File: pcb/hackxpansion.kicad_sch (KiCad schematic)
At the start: 0 parts

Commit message: added mcu and adc
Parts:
- added R1, R2: 27, symbol Device:R
- added R4: 1k, Resistor_SMD:R_0402_1005Metric, symbol Device:R
- added SW1: SW_Push, symbol Switch:SW_Push
- added U1: ADS131M08xPBS, Package_QFP:TQFP-32_5x5mm_P0.5mm, symbol Analog_ADC:ADS131M08xPBS
- added U2: RP2354B, Package_DFN_QFN:QFN-80-1EP_10x10mm_P0.4mm_EP3.4x3.4mm, symbol MCU_RaspberryPi:RP2354B
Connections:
- new net: R1.1, U2.66 (USB_DM)
- new net: U1.13 (AGND), U1.27 (AGND), U1.28 (AGND)
- new net: R4.1, SW1.1
- new net: SW1.2, U2.35 (RUN)
- new net: R2.1, U2.67 (USB_DP)
- new net: U2.10 (DVDD), U2.32 (DVDD), U2.51 (DVDD)
- new net: U2.15 (IOVDD), U2.24 (IOVDD), U2.29 (IOVDD), U2.41 (IOVDD), U2.5 (IOVDD), U2.50 (IOVDD), U2.60 (IOVDD), U2.76 (IOVDD)
- new net USB_D+: R2.2
- new net USB_D-: R1.2

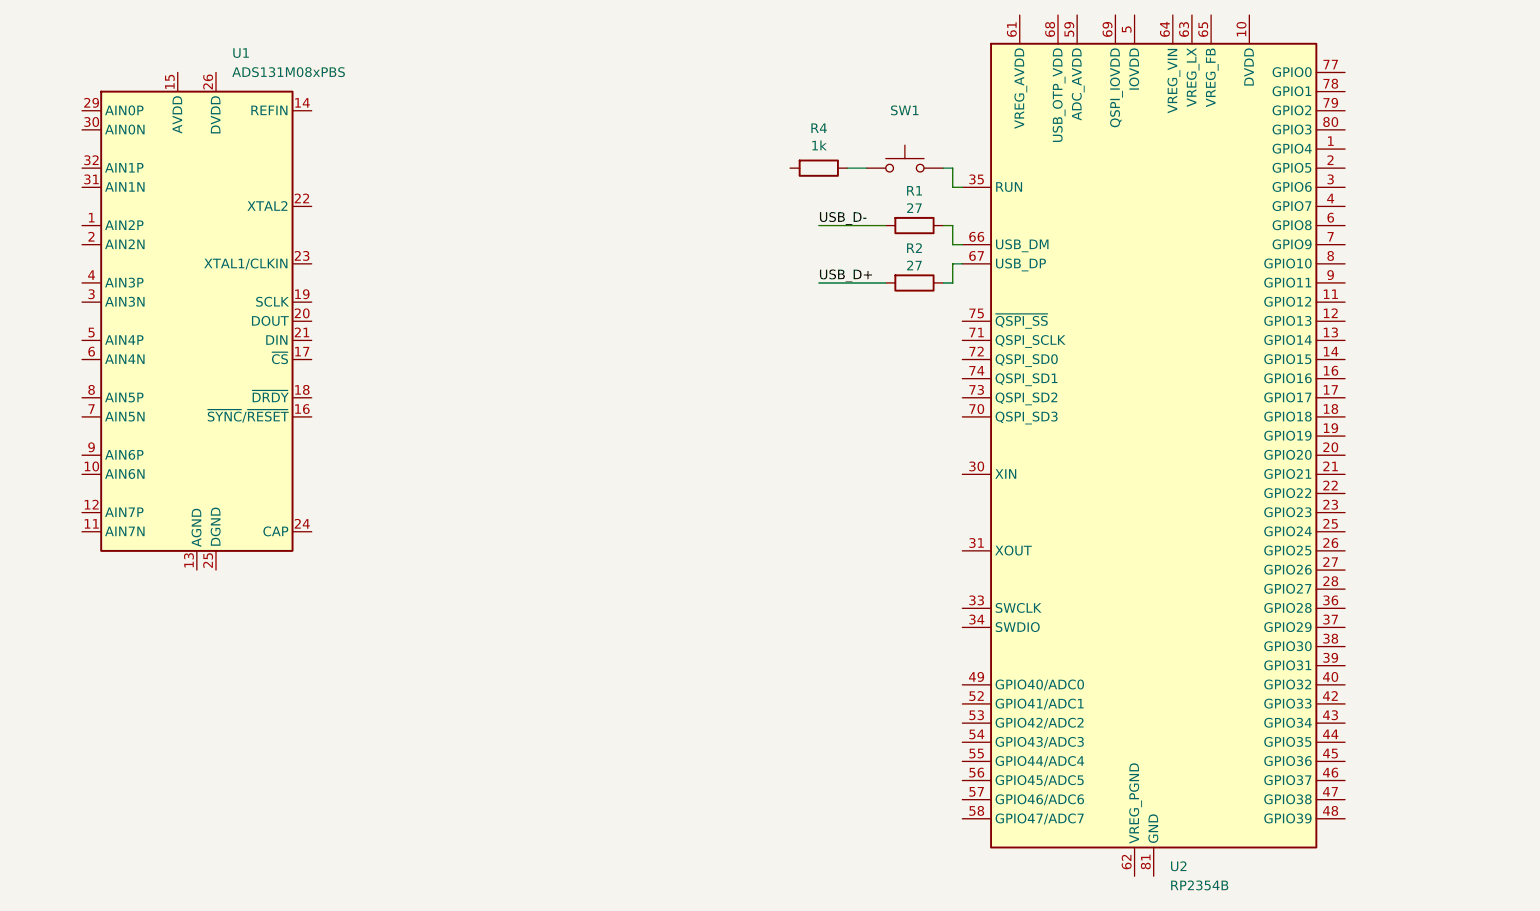
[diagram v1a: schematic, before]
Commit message: Added RP2354B and made basic fanout
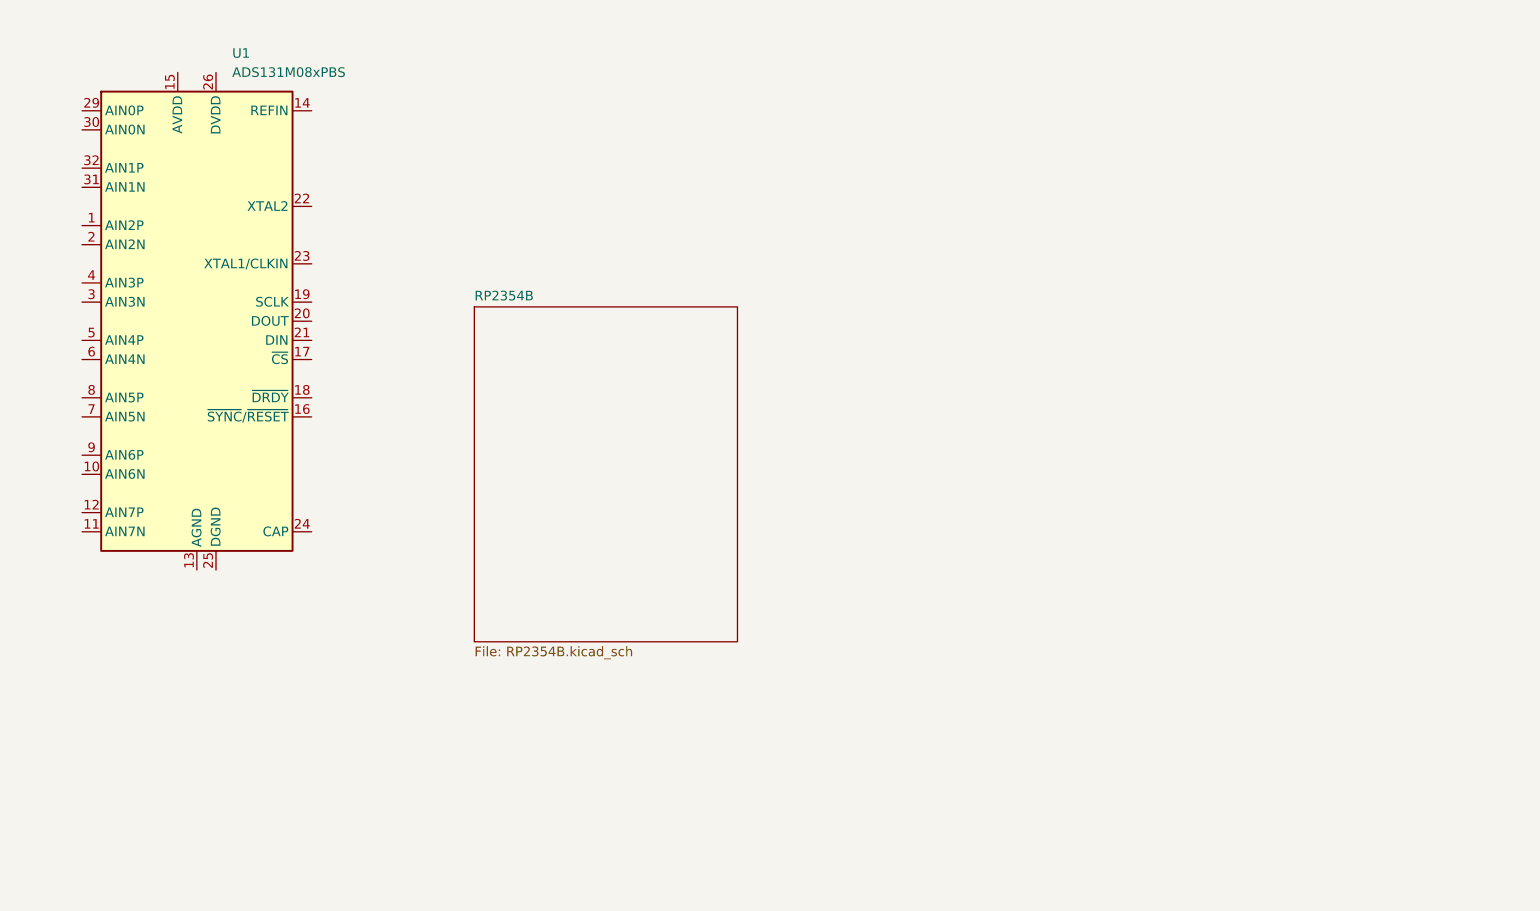
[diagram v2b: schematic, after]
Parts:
- removed R1, R2: 27, symbol Device:R
- removed R4: 1k, Resistor_SMD:R_0402_1005Metric, symbol Device:R
- removed SW1: SW_Push, symbol Switch:SW_Push
- removed U2: RP2354B, Package_DFN_QFN:QFN-80-1EP_10x10mm_P0.4mm_EP3.4x3.4mm, symbol MCU_RaspberryPi:RP2354B
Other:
- added sheet RP2354B (RP2354B.kicad_sch)

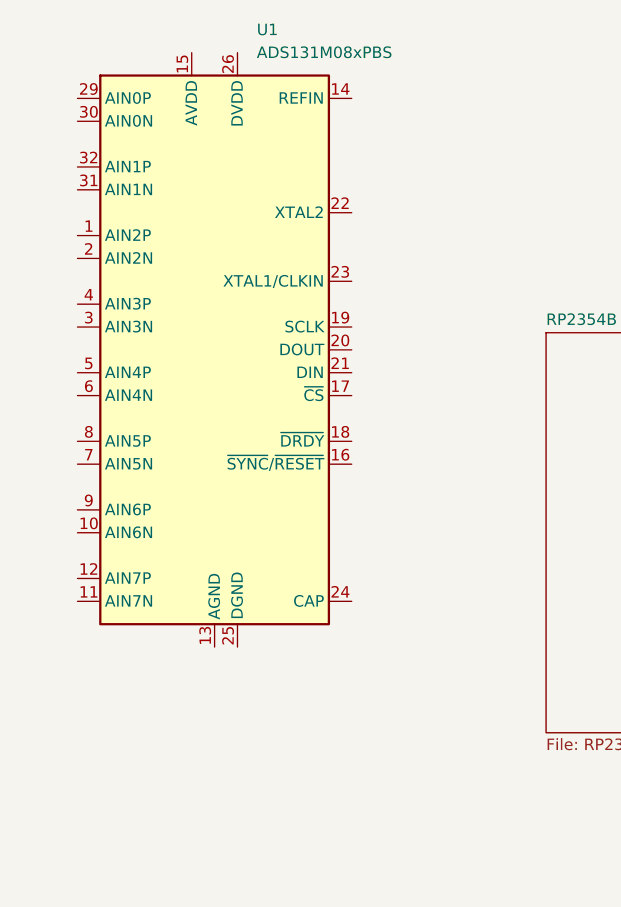
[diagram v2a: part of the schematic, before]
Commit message: Completed fanout
Completed the fanout for the rp2354B also placed the silkscreen labels in places where you can read them.
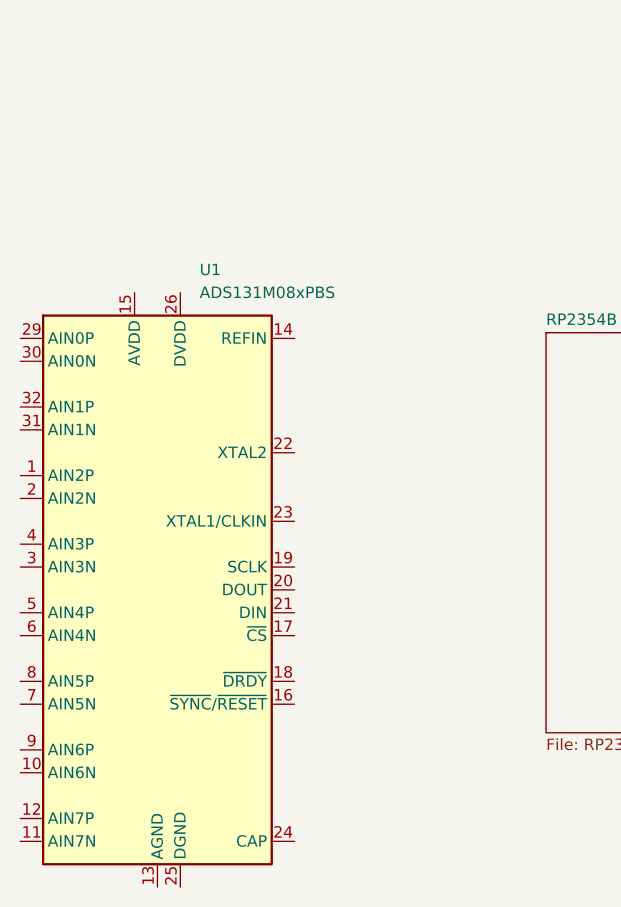
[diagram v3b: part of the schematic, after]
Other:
- moved on the sheet: U1
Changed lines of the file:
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@@
 	(symbol
 		(lib_id "Analog_ADC:ADS131M08xPBS")
-		(at 85.09 76.2 0)
+		(at 78.74 102.87 0)
 		(unit 1)
 		(exclude_from_sim no)
@@
 		(fields_autoplaced yes)
 		(property "Reference" "U1"
-			(at 89.7733 40.64 0)
+			(at 83.4233 67.31 0)
 			(effects
 				(font
@@
 		)
 		(property "Value" "ADS131M08xPBS"
-			(at 89.7733 43.18 0)
+			(at 83.4233 69.85 0)
 			(effects
 				(font
@@
 		)
 		(property "Footprint" "Package_QFP:TQFP-32_5x5mm_P0.5mm"
-			(at 135.89 132.08 0)
+			(at 129.54 158.75 0)
 			(effects
 				(font
@@
 		)
 		(property "Datasheet" "https://www.ti.com/lit/ds/symlink/ads131m08.pdf"
-			(at 135.89 134.62 0)
+			(at 129.54 161.29 0)
 			(effects
 				(font
@@
 		)
 		(property "Description" "8-channel, 24-bit, simultaneous sampling Delta-Sigma ADC, 32kSPS, G=1..128 PGA, SPI interface, integrated 1.2V reference, TQFP-32 (Texas PBS / S-PQFP-G32)"
-			(at 146.05 137.16 0)
+			(at 139.7 163.83 0)
 			(effects
 				(font

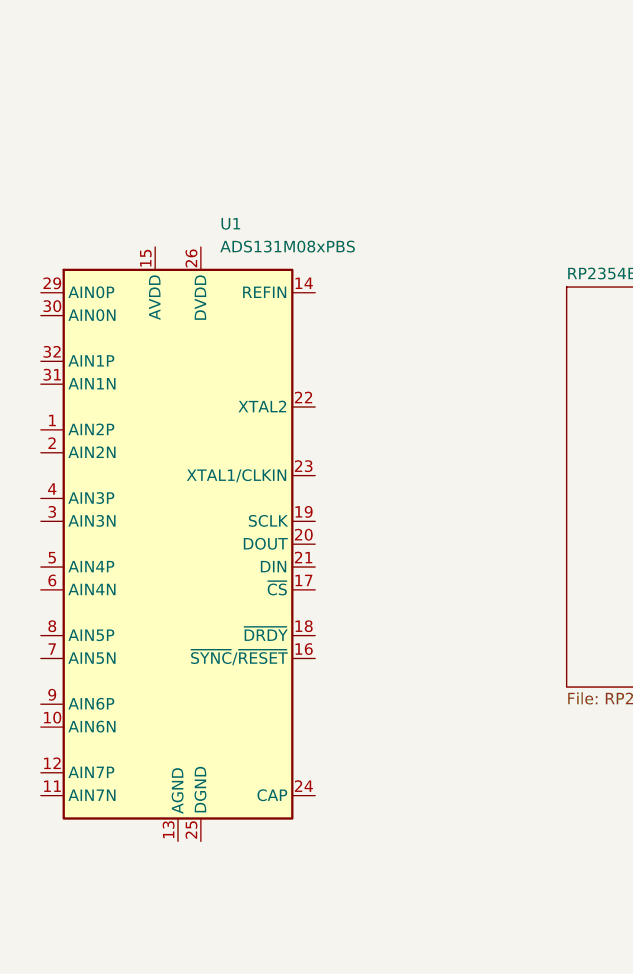
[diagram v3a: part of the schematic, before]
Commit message: ADC Power and input
Started with the power input and communication for the ADC
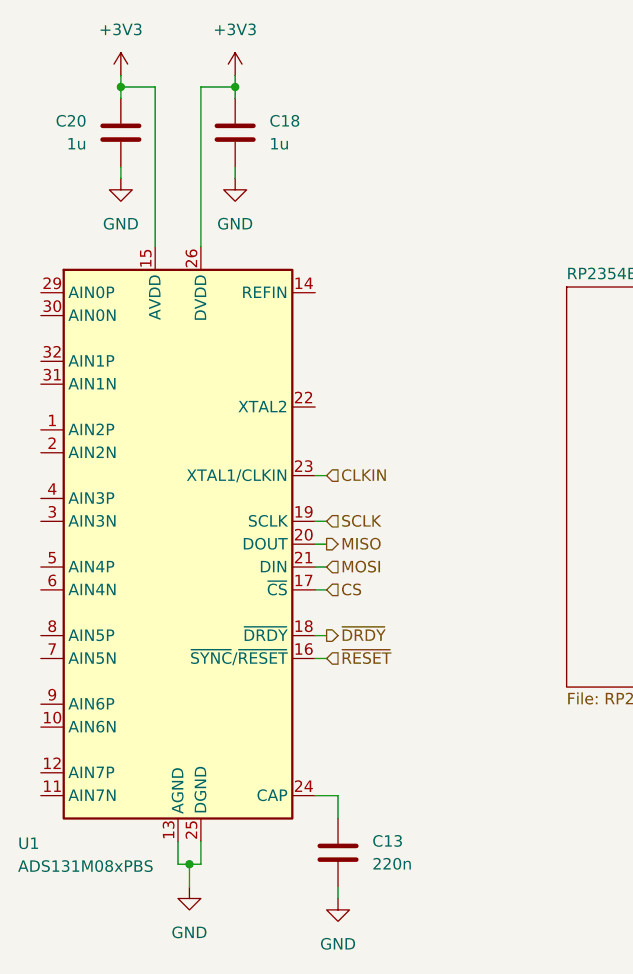
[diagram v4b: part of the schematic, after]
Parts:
- added C13: 220n, symbol Device:C
- added C18, C20: 1u, symbol Device:C
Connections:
- net GND: now reaches U1.13 (AGND), U1.27 (AGND), U1.28 (AGND)
- net GND: now also U1.25 (DGND), C13.2, C18.2, C20.2
- net +3V3: now reaches U1.15 (AVDD)
- net +3V3: now also U1.26 (DVDD), C18.1, C20.1
- net ~{RESET}: now reaches U1.16 (~{SYNC}/~{RESET})
- net CS: now reaches U1.17 (~{CS})
- net ~{DRDY}: now reaches U1.18 (~{DRDY})
- net SCLK: now reaches U1.19 (SCLK)
- net MISO: now reaches U1.20 (DOUT)
- net MOSI: now reaches U1.21 (DIN)
- net CLKIN: now reaches U1.23 (XTAL1/CLKIN)
- net at U1.24 (CAP): now also C13.1

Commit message: Fixed missing stuff and now finally separate sheet for the ADC
Auto stash before merge of "main" and "origin/main"
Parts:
- removed C13: 220n, symbol Device:C
- removed C18, C20: 1u, symbol Device:C
- removed U1: ADS131M08xPBS, Package_QFP:TQFP-32_5x5mm_P0.5mm, symbol Analog_ADC:ADS131M08xPBS
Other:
- added sheet ADC (ADC.kicad_sch)

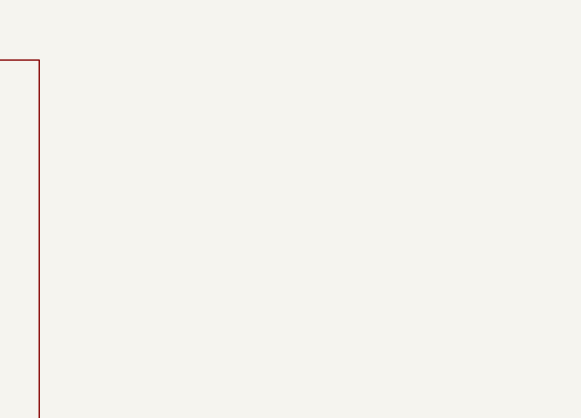
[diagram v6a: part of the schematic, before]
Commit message: added new adc symbol
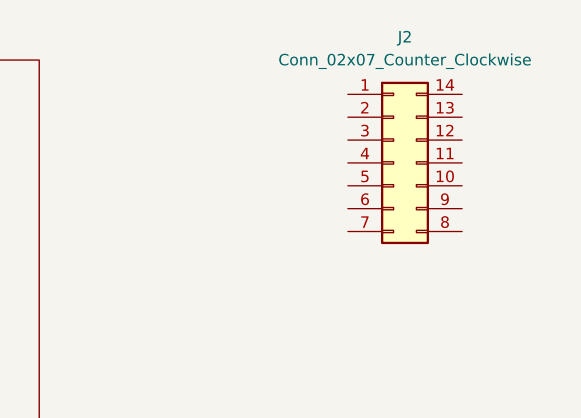
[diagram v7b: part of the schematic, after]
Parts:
- added J2: Conn_02x07_Counter_Clockwise, Connector_PinSocket_2.54mm:PinSocket_2x07_P2.54mm_Horizontal, symbol Connector_Generic:Conn_02x07_Counter_Clockwise
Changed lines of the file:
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@@
 	(generator_version "10.0")
 	(paper "A4")
+	(symbol
+		(lib_id "Connector_Generic:Conn_02x07_Counter_Clockwise")
+		(at 242.57 87.63 0)
+		(unit 1)
+		(body_style 1)
+		(exclude_from_sim no)
+		(in_bom yes)
+		(on_board yes)
+		(in_pos_files yes)
+		(dnp no)
+		(fields_autoplaced yes)
+		(property "Reference" "J2"
+			(at 243.84 73.66 0)
+			(show_name no)
+			(do_not_autoplace no)
+			(effects
+				(font
+					(size 1.27 1.27)
+				)
+			)
+		)
+		(property "Value" "Conn_02x07_Counter_Clockwise"
+			(at 243.84 76.2 0)
+			(show_name no)
+			(do_not_autoplace no)
+			(effects
+				(font
+					(size 1.27 1.27)
+				)
+			)
+		)
+		(property "Footprint" "Connector_PinSocket_2.54mm:PinSocket_2x07_P2.54mm_Horizontal"
+			(at 242.57 87.63 0)
+			(hide yes)
+			(show_name no)
+			(do_not_autoplace no)
+			(effects
+				(font
+					(size 1.27 1.27)
+				)
+			)
+		)
+		(property "Datasheet" ""
+			(at 242.57 87.63 0)
+			(hide yes)
+			(show_name no)
+			(do_not_autoplace no)
+			(effects
+				(font
+					(size 1.27 1.27)
+				)
+			)
+		)
+		(property "Description" "Generic connector, double row, 02x07, counter clockwise pin numbering scheme (similar to DIP package numbering), script generated (kicad-library-utils/schlib/autogen/connector/)"
+			(at 242.57 87.63 0)
+			(hide yes)
+			(show_name no)
+			(do_not_autoplace no)
+			(effects
+				(font
+					(size 1.27 1.27)
+				)
+			)
+		)
+		(pin "4"
+		)
+		(pin "10"
+		)
+		(pin "1"
+		)
+		(pin "11"
+		)
+		(pin "3"
+		)
+		(pin "2"
+		)
+		(pin "7"
+		)
+		(pin "9"
+		)
+		(pin "12"
+		)
+		(pin "14"
+		)
+		(pin "5"
+		)
+		(pin "13"
+		)
+		(pin "8"
+		)
+		(pin "6"
+		)
+		(instances
+			(project "hackxpansion"
+				(path "/aaf5804d-3f78-442b-969e-39faa388db94"
+					(reference "J2")
+					(unit 1)
+				)
+			)
+		)
+	)
 	(sheet
 		(at 121.92 74.295)

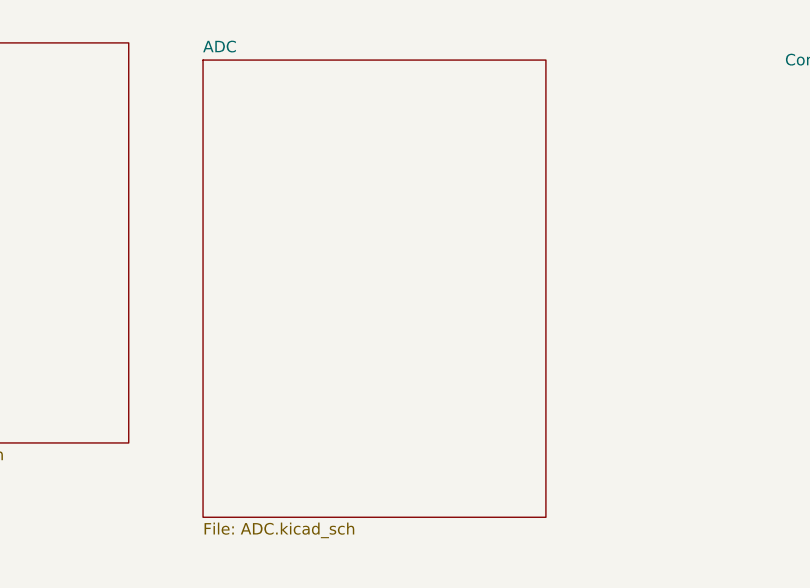
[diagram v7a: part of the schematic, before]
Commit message: finished adding new adc, and started on dispaly
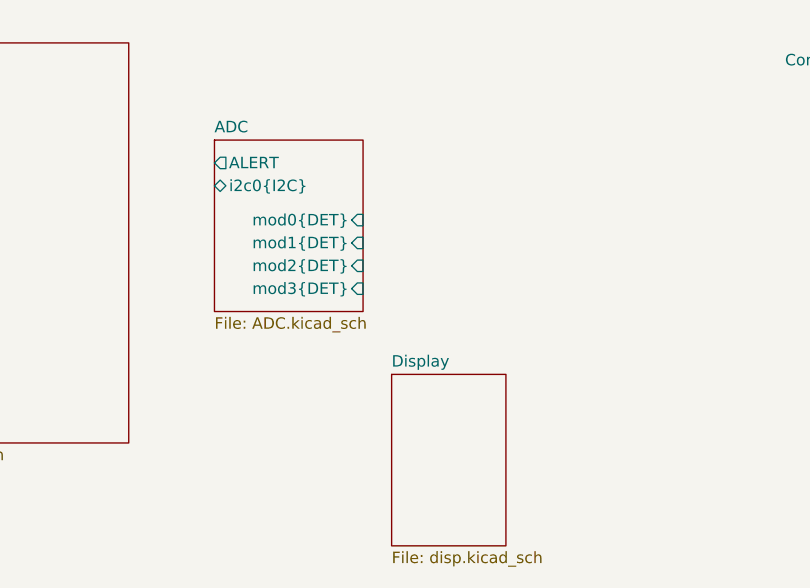
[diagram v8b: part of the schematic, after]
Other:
- added sheet Display (disp.kicad_sch)
- sheet ADC ports: added ALERT, i2c0{I2C}, mod0{DET}, mod1{DET}, mod2{DET}, mod3{DET}; removed none
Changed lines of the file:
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@@
 	)
 	(sheet
-		(at 165.1 76.2)
-		(size 38.1 50.8)
+		(at 186.055 111.125)
+		(size 12.7 19.05)
+		(exclude_from_sim no)
+		(in_bom yes)
+		(on_board yes)
+		(dnp no)
+		(fields_autoplaced yes)
+		(stroke
+			(width 0.1524)
+			(type solid)
+		)
+		(fill
+			(color 0 0 0 0)
+		)
+		(property "Sheetname" "Display"
+			(at 186.055 110.4134 0)
+			(show_name no)
+			(do_not_autoplace no)
+			(effects
+				(font
+					(size 1.27 1.27)
+				)
+				(justify left bottom)
+			)
+		)
+		(property "Sheetfile" "disp.kicad_sch"
+			(at 186.055 130.7596 0)
+			(show_name no)
+			(do_not_autoplace no)
+			(effects
+				(font
+					(size 1.27 1.27)
+				)
+				(justify left top)
+			)
+		)
+		(instances
+			(project "hackxpansion"
+				(path "/aaf5804d-3f78-442b-969e-39faa388db94"
+					(page "4")
+				)
+			)
+		)
+	)
+	(sheet
+		(at 166.37 85.09)
+		(size 16.51 19.05)
 		(exclude_from_sim no)
 		(in_bom yes)
@@
 		)
 		(property "Sheetname" "ADC"
-			(at 165.1 75.4884 0)
+			(at 166.37 84.3784 0)
 			(show_name no)
 			(do_not_autoplace no)
@@
 		)
 		(property "Sheetfile" "ADC.kicad_sch"
-			(at 165.1 127.5846 0)
+			(at 166.37 104.7246 0)
 			(show_name no)
 			(do_not_autoplace no)
@@
 			)
 		)
+		(pin "ALERT" output
+			(at 166.37 87.63 180)
+			(effects
+				(font
+					(size 1.27 1.27)
+				)
+				(justify left)
+			)
+		)
+		(pin "i2c0{I2C}" bidirectional
+			(at 166.37 90.17 180)
+			(effects
+				(font
+					(size 1.27 1.27)
+				)
+				(justify left)
+			)
+		)
+		(pin "mod0{DET}" input
+			(at 182.88 93.98 0)
+			(effects
+				(font
+					(size 1.27 1.27)
+				)
+				(justify right)
+			)
+		)
+		(pin "mod1{DET}" input
+			(at 182.88 96.52 0)
+			(effects
+				(font
+					(size 1.27 1.27)
+				)
+				(justify right)
+			)
+		)
+		(pin "mod2{DET}" input
+			(at 182.88 99.06 0)
+			(effects
+				(font
+					(size 1.27 1.27)
+				)
+				(justify right)
+			)
+		)
+		(pin "mod3{DET}" input
+			(at 182.88 101.6 0)
+			(effects
+				(font
+					(size 1.27 1.27)
+				)
+				(justify right)
+			)
+		)
